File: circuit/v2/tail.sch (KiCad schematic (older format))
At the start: 71 parts, among them J1 RADIO_RST_EN, J10 BATT_MON, J11 UART, J12 VREG_PWR, J13 I_MEASURE, J14 MCU_PWR, J15 PWR_EXT, J16 EXT_PWR, J17 RADIO_PWR, J18 PWR_LIPO, J19 LiPo, J2 PULLUP_SELECT, J20 RADIOAON_PWR, J21 PWR_COIN, J22 ACCEL_PWR, J23 PWR_USB, J24 CHG_EN, J25 USB_OTG, J3 TXLED, J4 RXLED, J5 RXOKLED, J6 SFDLED, J7 RADIO_GPIO, J8 GPIO, J9 DEBUG, Q1 Q_NMOS_GSD, U1 DWM1000, U2 EFM32HG222F64, U3 MC3630, U4 XC6215B332NR, U5 MCP73831-2-OT, Y1 32.768kHz CFPX-217 20ppm 7pF, Y2 E3SB16.0000F09G11AE

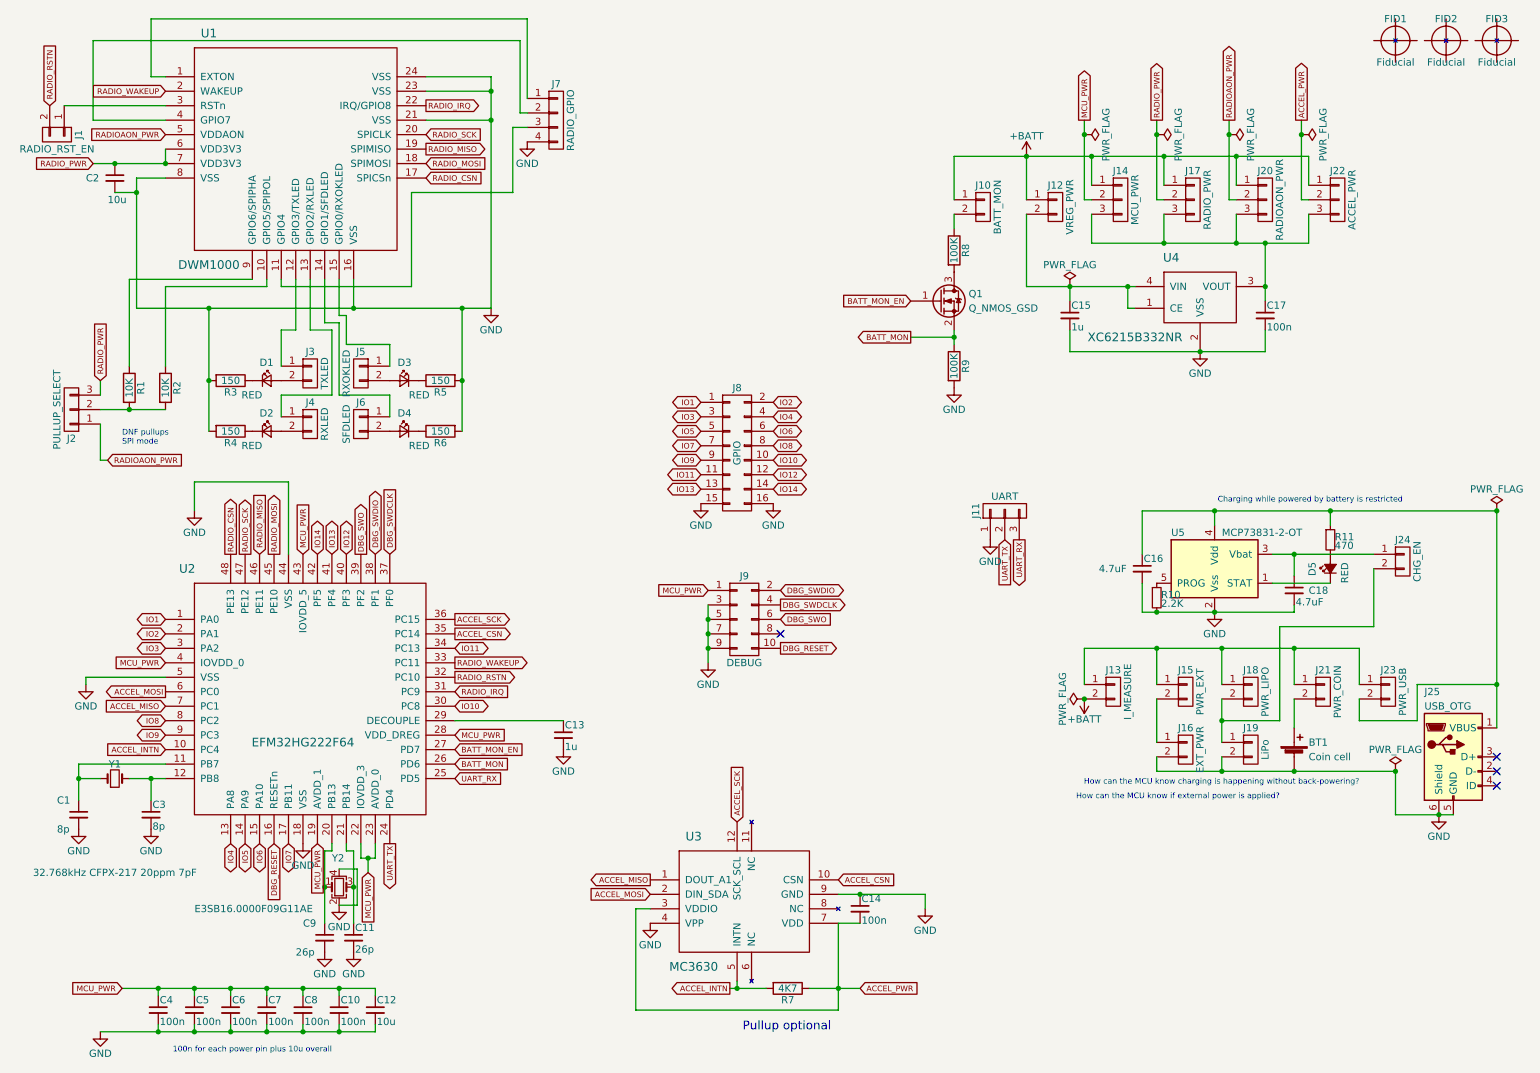
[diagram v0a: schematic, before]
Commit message: tail: Remove jumper and unnecessary components and move accel spi pins
Signed-off-by: Gavan Fantom <gavan.fantom@unipart.io>
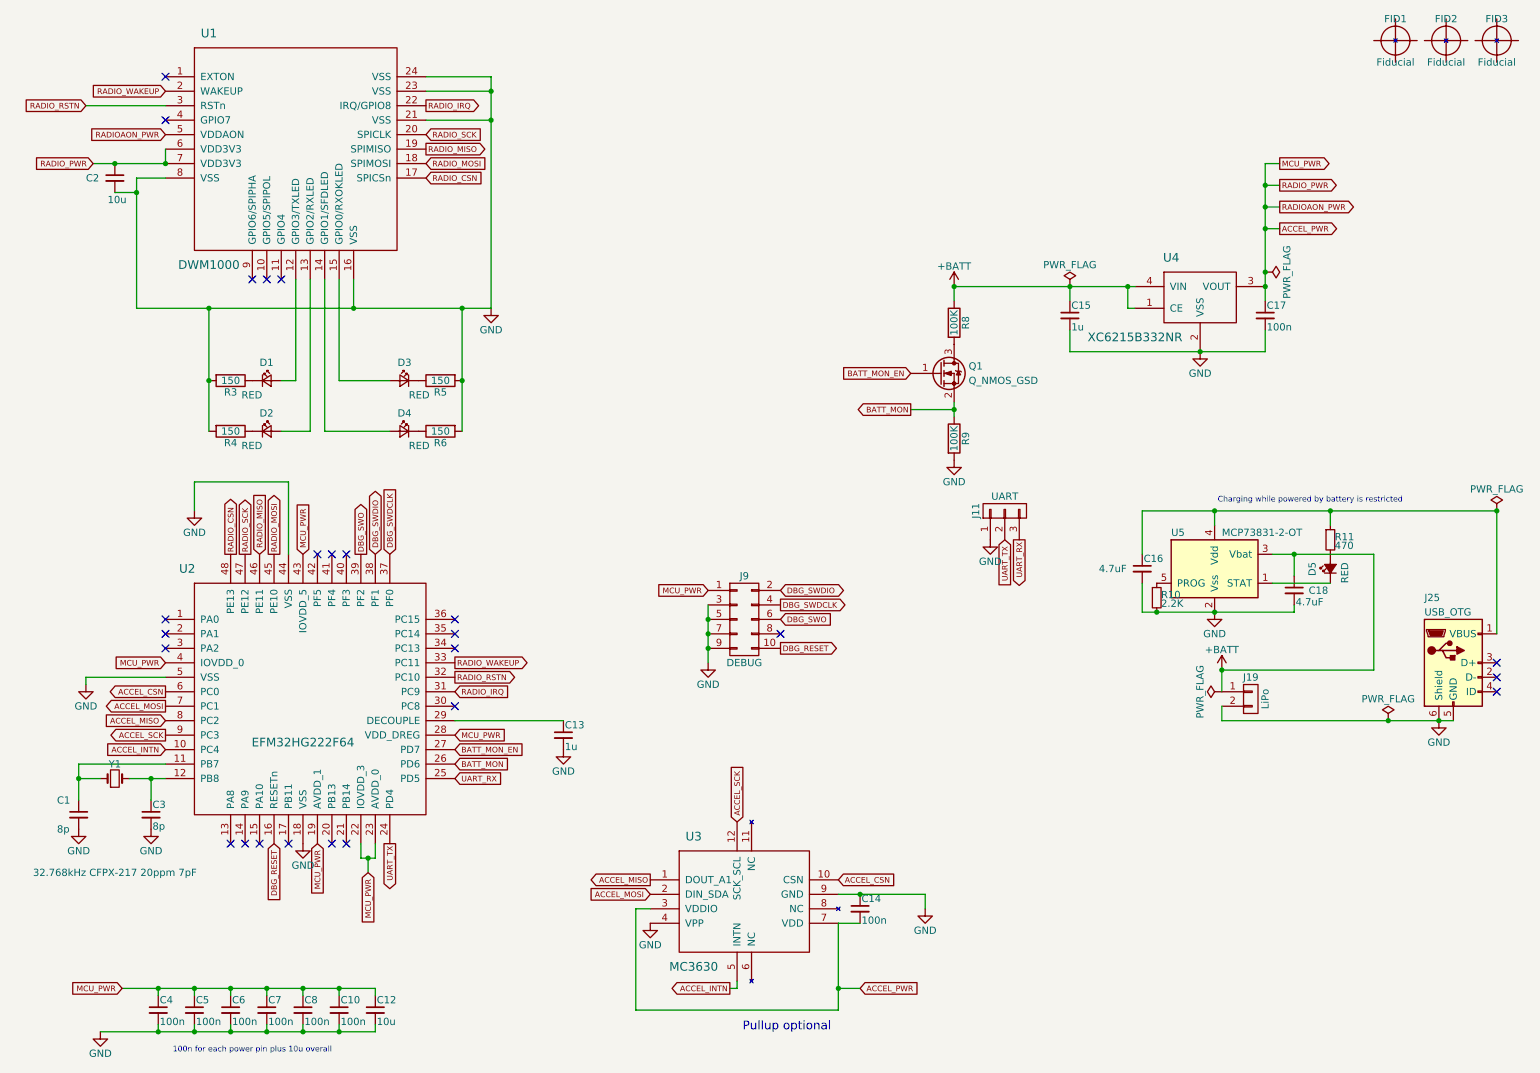
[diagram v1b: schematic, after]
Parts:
- removed BT1: Coin cell, Battery_Holders:Keystone_105_1x2430-CoinCell, symbol Battery_Cell
- removed C11, C9: 26p, Capacitors_SMD:C_0603, symbol C_Small
- removed J1: RADIO_RST_EN, Pin_Headers:Pin_Header_Straight_1x02_Pitch2.54mm, symbol CONN_01X02
- removed J10: BATT_MON, Pin_Headers:Pin_Header_Straight_1x02_Pitch2.54mm, symbol CONN_01X02
- removed J12: VREG_PWR, Pin_Headers:Pin_Header_Straight_1x02_Pitch2.54mm, symbol CONN_01X02
- removed J13: I_MEASURE, Pin_Headers:Pin_Header_Straight_1x02_Pitch2.54mm, symbol CONN_01X02
- removed J14: MCU_PWR, Pin_Headers:Pin_Header_Straight_1x03_Pitch2.54mm, symbol CONN_01X03
- removed J15: PWR_EXT, Pin_Headers:Pin_Header_Straight_1x02_Pitch2.54mm, symbol CONN_01X02
- removed J16: EXT_PWR, Pin_Headers:Pin_Header_Straight_1x02_Pitch2.54mm, symbol CONN_01X02
- removed J17: RADIO_PWR, Pin_Headers:Pin_Header_Straight_1x03_Pitch2.54mm, symbol CONN_01X03
- removed J18: PWR_LIPO, Pin_Headers:Pin_Header_Straight_1x02_Pitch2.54mm, symbol CONN_01X02
- removed J2: PULLUP_SELECT, Pin_Headers:Pin_Header_Straight_1x03_Pitch2.54mm, symbol CONN_01X03
- removed J20: RADIOAON_PWR, Pin_Headers:Pin_Header_Straight_1x03_Pitch2.54mm, symbol CONN_01X03
- removed J21: PWR_COIN, Pin_Headers:Pin_Header_Straight_1x02_Pitch2.54mm, symbol CONN_01X02
- removed J22: ACCEL_PWR, Pin_Headers:Pin_Header_Straight_1x03_Pitch2.54mm, symbol CONN_01X03
- removed J23: PWR_USB, Pin_Headers:Pin_Header_Straight_1x02_Pitch2.54mm, symbol CONN_01X02
- removed J24: CHG_EN, Pin_Headers:Pin_Header_Straight_1x02_Pitch2.54mm, symbol CONN_01X02
- removed J3: TXLED, Pin_Headers:Pin_Header_Straight_1x02_Pitch2.54mm, symbol CONN_01X02
- removed J4: RXLED, Pin_Headers:Pin_Header_Straight_1x02_Pitch2.54mm, symbol CONN_01X02
- removed J5: RXOKLED, Pin_Headers:Pin_Header_Straight_1x02_Pitch2.54mm, symbol CONN_01X02
- removed J6: SFDLED, Pin_Headers:Pin_Header_Straight_1x02_Pitch2.54mm, symbol CONN_01X02
- removed J7: RADIO_GPIO, Pin_Headers:Pin_Header_Straight_1x04_Pitch2.54mm, symbol CONN_01X04
- removed J8: GPIO, Pin_Headers:Pin_Header_Straight_2x08_Pitch2.54mm, symbol CONN_02X08
- removed R1, R2: 10K, Resistors_SMD:R_0603, symbol R
- removed R7: 4K7, Resistors_SMD:R_0603, symbol R
- removed Y2: E3SB16.0000F09G11AE, Crystals:Crystal_SMD_3225-4pin_3.2x2.5mm, symbol Crystal_GND24_Small
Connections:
- net IO8 is gone; now on net ACCEL_MISO: U2.8 (PC2)
- net IO9 is gone; now on net ACCEL_SCK: U2.9 (PC3)
- net MCU_PWR is gone; now on net ACCEL_PWR: C10.1, C12.1, C4.1, C5.1, C6.1, C7.1, C8.1, J9.1 (P1), U2.19 (AVDD_1), U2.22 (IOVDD_3), U2.23 (AVDD_0), U2.28 (VDD_DREG), U2.4 (IOVDD_0), U2.43 (IOVDD_5)
- net RADIOAON_PWR is gone; now on net ACCEL_PWR: U1.5 (VDDAON)
- net RADIO_PWR is gone; now on net ACCEL_PWR: C2.1, U1.6 (VDD3V3), U1.7 (VDD3V3)
- net +BATT: now also C15.1, C18.1, J19.1 (P1), R8.1, U4.1 (CE), U4.4 (VIN), U5.3 (Vbat)
- net ACCEL_CSN: now also U2.6 (PC0); no longer U2.35 (PC14)
- net ACCEL_MISO: no longer U2.7 (PC1)
- net ACCEL_MOSI: now also U2.7 (PC1); no longer U2.6 (PC0)
- net ACCEL_PWR: now also C17.1, U4.3 (VOUT)
- net ACCEL_SCK: no longer U2.36 (PC15)
- net RADIO_RSTN: now also U1.3 (RSTn)
- net at U1.12 (GPIO3/TXLED): now also D1.2 (A)
- net at U1.13 (GPIO2/RXLED): now also D2.2 (A)
- net at U1.14 (GPIO1/SFDLED): now also D4.2 (A)
- net at U1.15 (GPIO0/RXOKLED): now also D3.2 (A)
- net IO1: no longer names the net of U2.1 (PA0)
- net IO10: no longer names the net of U2.30 (PC8)
- net IO11: no longer names the net of U2.34 (PC13)
- net IO12: no longer names the net of U2.40 (PF3)
- net IO13: no longer names the net of U2.41 (PF4)
- net IO14: no longer names the net of U2.42 (PF5)
- net IO2: no longer names the net of U2.2 (PA1)
- net IO3: no longer names the net of U2.3 (PA2)
- net IO4: no longer names the net of U2.13 (PA8)
- net IO5: no longer names the net of U2.14 (PA9)
- net IO6: no longer names the net of U2.15 (PA10)
- net IO7: no longer names the net of U2.17 (PB11)
- no-connect marks 4 -> 25
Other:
- note removed: "DNF pullups\nSPI mode"
- note removed: "How can the MCU know charging is happening without back-powering?"
- note removed: "How can the MCU know if external power is applied?"
- moved on the sheet: J19, J25, Q1, R8, R9

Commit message: tail: Sort out BOM and fix ERC
Signed-off-by: Gavan Fantom <gavan.fantom@unipart.io>
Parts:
- C1, C3: MFR (none) -> Multicomp; MPN (none) -> MC0603N8R0D500CT; SPN (none) -> 1759051; SPR (none) -> Farnell; SPURL (none) -> -
- C10, C14, C17, C4, C5, C6, C7, C8: MFR (none) -> Multicomp; MPN (none) -> MC0603B104K500CT; SPN (none) -> 1759122; SPR (none) -> Farnell; SPURL (none) -> -
- C12, C2: MFR (none) -> Murata; MPN (none) -> ZRB18AR61E106ME01L; SPN (none) -> 2469398; SPR (none) -> Farnell; SPURL (none) -> -
- C13, C15: MFR (none) -> Multicomp; MPN (none) -> MC0603B105K160CT; SPN (none) -> 2320814; SPR (none) -> Farnell; SPURL (none) -> -
- C16, C18: MFR (none) -> Murata; MPN (none) -> GRM188R60J475ME19D; SPN (none) -> 2362095; SPR (none) -> Farnell; SPURL (none) -> -
- D1, D2, D3, D4, D5: MFR (none) -> Kingbright; MPN (none) -> KP-1608SURCK; SPN (none) -> 2290329; SPR (none) -> Farnell; SPURL (none) -> -
- FID1, FID2, FID3: MFR (none) -> -; MPN (none) -> -; SPN (none) -> -; SPR (none) -> -; SPURL (none) -> -
- J11: MFR (none) -> Multicomp; MPN (none) -> 2211S-03G; SPN (none) -> 1593412; SPR (none) -> Farnell; SPURL (none) -> -
- J19: MFR (none) -> JST; MPN (none) -> S2B-PH-K-S (LF)(SN); SPN (none) -> 9491902; SPR (none) -> Farnell; SPURL (none) -> -
- J25: MFR (none) -> Molex; MPN (none) -> 47346-0001; SPN (none) -> 1568026; SPR (none) -> Farnell; SPURL (none) -> -
- J9: MFR (none) -> Samtec; MPN (none) -> FTSH-105-01-L-DV; SPN (none) -> 1667759; SPR (none) -> Farnell; SPURL (none) -> -
- Q1: MFR (none) -> Nexperia; MPN (none) -> NX3020NAKW; SPN (none) -> 2311183; SPR (none) -> Farnell; SPURL (none) -> -
- R10: MFR (none) -> Multicomp; MPN (none) -> MCWR06X2201FTL; SPN (none) -> 2447320; SPR (none) -> Farnell; SPURL (none) -> -
- R11: MFR (none) -> Multicomp; MPN (none) -> MCWR06X4700FTL; SPN (none) -> 2447374; SPR (none) -> Farnell; SPURL (none) -> -
- R3, R4, R5, R6: MFR (none) -> Multicomp; MPN (none) -> MCWR06X1500FTL; SPN (none) -> 2447255; SPR (none) -> Farnell; SPURL (none) -> -
- R8, R9: MFR (none) -> Multicomp; MPN (none) -> MCWR06X1003FTL; SPN (none) -> 2447226; SPR (none) -> Farnell; SPURL (none) -> -
- U1: MFR (none) -> Decawave; MPN (none) -> DWM1000; SPN (none) -> 1479-1002-1-ND; SPR (none) -> DigiKey; SPURL (none) -> -
- U2: MFR (none) -> Silicon Labs; MPN (none) -> EFM32HG222F64G-B-QFP48; SPN (none) -> 634-HG222F64GBQFP48; SPR (none) -> Mouser; SPURL (none) -> -
- U3: MFR (none) -> mCube; MPN (none) -> MC3630; SPN (none) -> 498-MC3630; SPR (none) -> Mouser; SPURL (none) -> -
- U4: MFR (none) -> Torex; MPN (none) -> XC6215B332NR; SPN (none) -> 1057811; SPR (none) -> Farnell; SPURL (none) -> -
- U5: MFR (none) -> Microchip; MPN (none) -> MCP73831T-2ACI/OT; SPN (none) -> 1332158; SPR (none) -> Farnell; SPURL (none) -> -
- Y1: MFR (none) -> IQD Frequency Products; MPN (none) -> LFXTAL009709; SPN (none) -> 2449501; SPR (none) -> Farnell; SPURL (none) -> -
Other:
- note removed: "Pullup optional"

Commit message: tail: Add power switch
Signed-off-by: Gavan Fantom <gavan.fantom@unipart.io>
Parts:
- added SW1: SW_SPDT, symbol SW_SPDT
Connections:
- net +BATT: now also SW1.3 (C); no longer C18.1, J19.1 (P1), U5.3 (Vbat)
- new net: C18.1, J19.1 (P1), SW1.2 (B), U5.3 (Vbat)
- no-connect marks 25 -> 26
